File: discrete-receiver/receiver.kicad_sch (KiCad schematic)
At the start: 22 parts, among them J1 His Excellence, J3 External Filter, J7 Her Excellency, T1 H1102NLT, T2 MABA-007159-000000, U5 ADE-1+

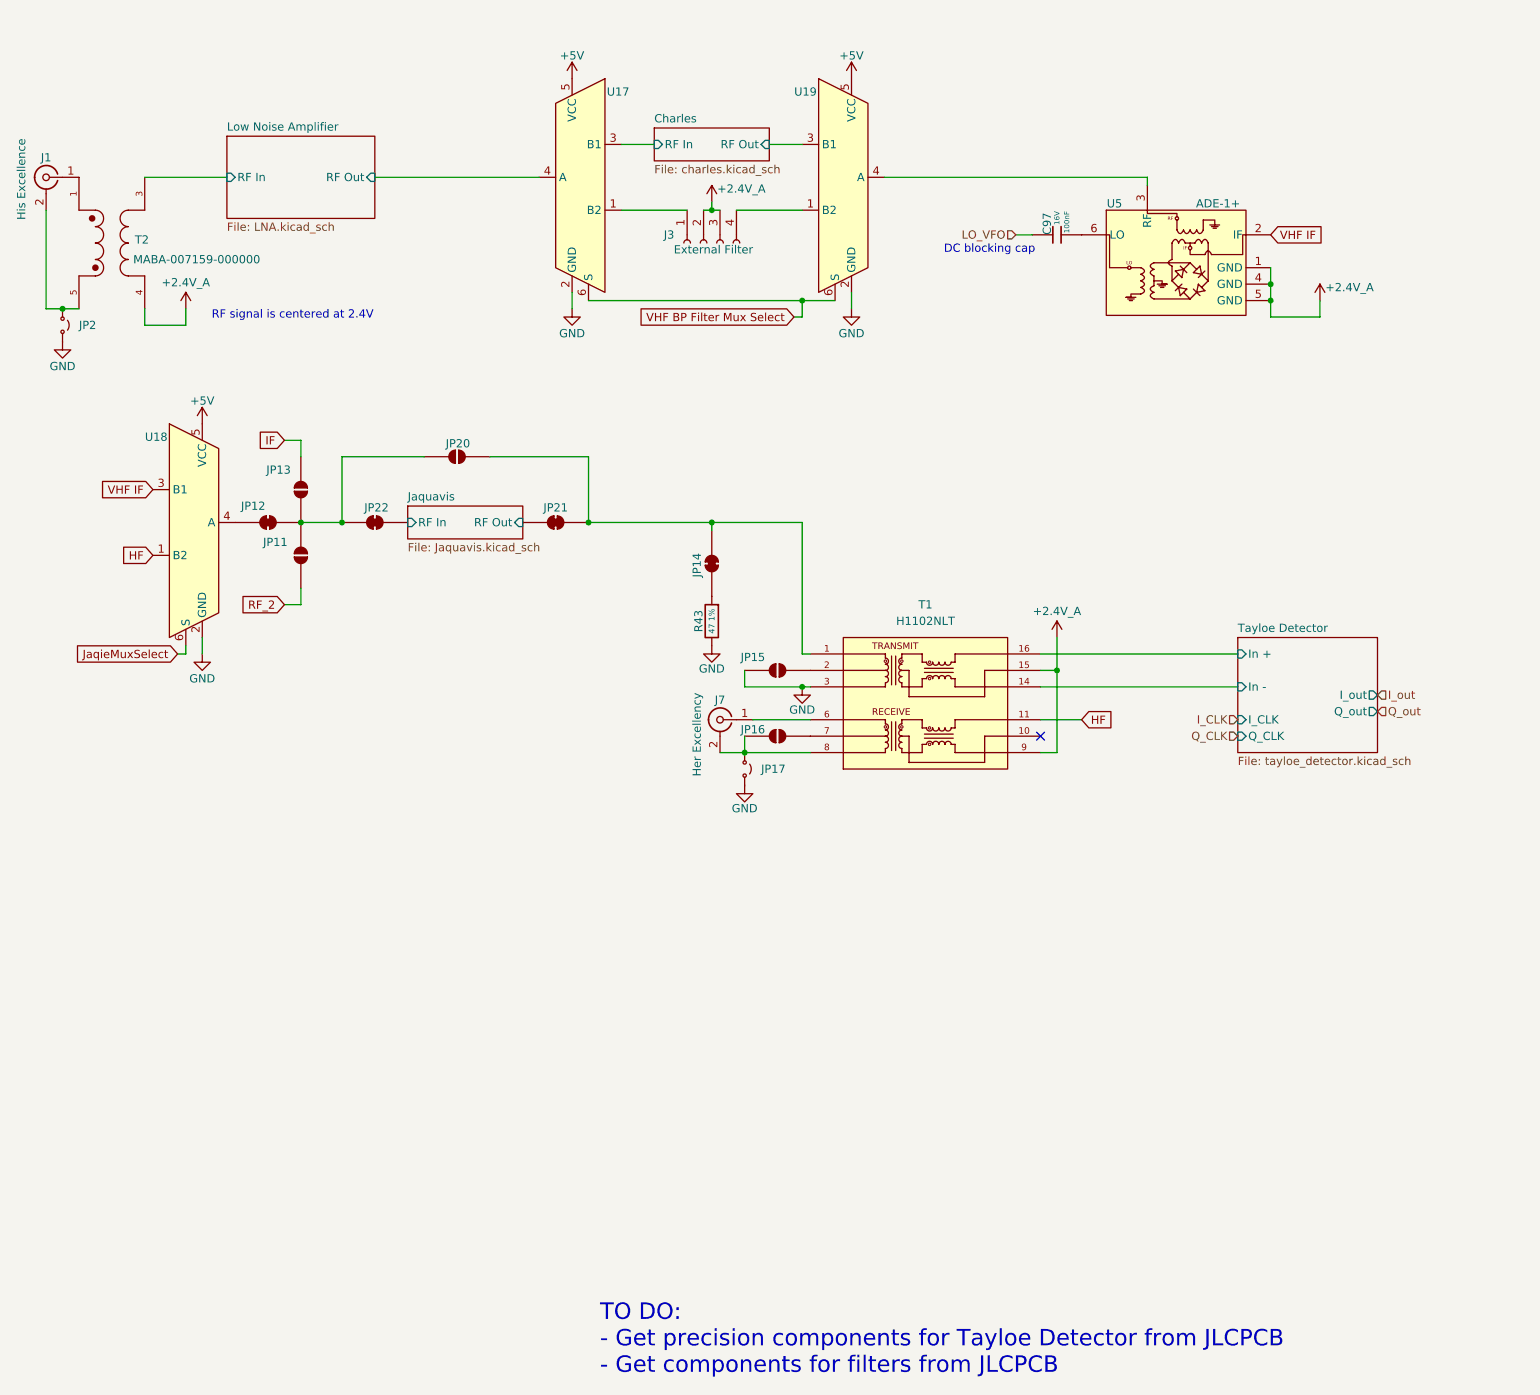
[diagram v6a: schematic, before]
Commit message: Added bypass capacitors to places on the 2.4V_A bus.
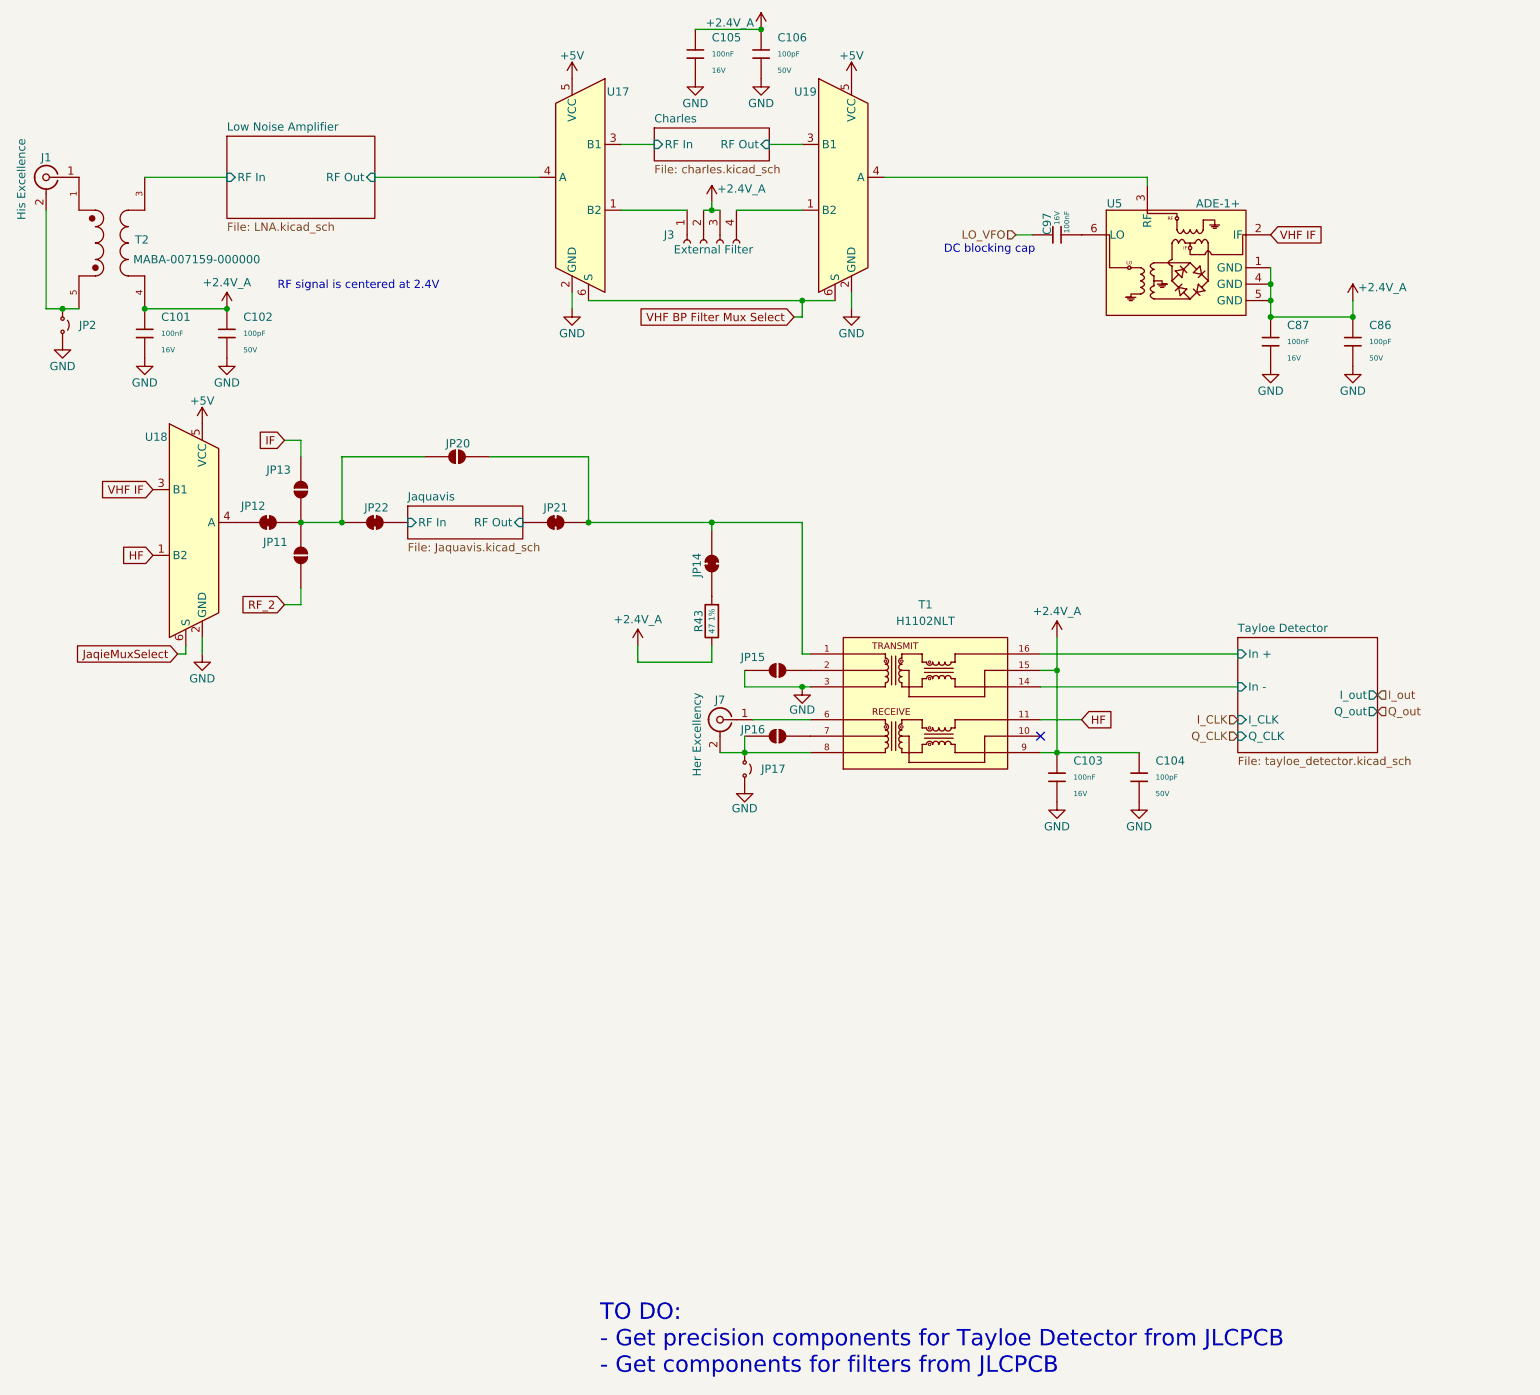
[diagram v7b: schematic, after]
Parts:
- added C101, C103, C105, C87: 100nF, PCM_JLCPCB:C_0402, symbol PCM_JLCPCB-Capacitors:0402,100nF
- added C102, C104, C106, C86: 100pF, PCM_JLCPCB:C_0603, symbol PCM_JLCPCB-Capacitors:0603,100pF
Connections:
- net +2.4V_A: now also R43.1, C101.1, C102.1, C103.1, C104.1, C105.1, C106.1, C86.1, C87.1
- net GND: now also C101.2, C102.2, C103.2, C104.2, C105.2, C106.2, C86.2, C87.2; no longer R43.1

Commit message: all parts now have footprints
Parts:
- J1, J7: footprint (none) -> Connector_Coaxial:BNC_TEConnectivity_1478204_Vertical
- J3: footprint (none) -> Connector_PinHeader_2.54mm:PinHeader_1x04_P2.54mm_Vertical
- JP11, JP13, JP15, JP16, JP20: footprint (none) -> Jumper:SolderJumper-2_P1.3mm_Open_Pad1.0x1.5mm
- JP12, JP14, JP21, JP22: footprint (none) -> Jumper:SolderJumper-2_P1.3mm_Bridged_RoundedPad1.0x1.5mm
- T1: footprint H1102NLT:XFMR_H1102NLT -> sdr_project:XFMR_H1102NLT
- T2: footprint MABA-007159-000000:XFMR_MABA-007159-000000 -> sdr_project:XFMR_MABA-007159-000000
